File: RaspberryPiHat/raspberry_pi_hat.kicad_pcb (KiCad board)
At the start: 2 copper layers, 65 x 56 mm, 11 parts, among them J1 CONN_2x20_FEM_100PITCH_635INS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, U1 CAT24C32

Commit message: rework done
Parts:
- C1: value 100nF_0603_50V -> 100nF_CER_0603_50V
- J1: footprint JB_Header_100mils:ESQ-120-34-G-D -> ENYA_Header_100mils:ESQ-120-34-G-D

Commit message: updating project templates
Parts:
- J1: value CONN_2x20_FEM_100PITCH_635INS_280POST -> CONN_2x20_FEM_100PITCH_335INS_126POST; footprint ENYA_Header_100mils:ESQ-120-34-G-D -> ENYA_Header_100mils:PPTC202LFBN-RC; moved to F.Cu
- turned J1 to 90 degrees
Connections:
- J1 pad 10: Net-(J1-Pad10) -> (no net)
- J1 pad 11: Net-(J1-Pad11) -> (no net)
- J1 pad 12: Net-(J1-Pad12) -> (no net)
- J1 pad 13: Net-(J1-Pad13) -> (no net)
- J1 pad 15: Net-(J1-Pad15) -> (no net)
- J1 pad 16: Net-(J1-Pad16) -> (no net)
- J1 pad 18: Net-(J1-Pad18) -> (no net)
- J1 pad 19: Net-(J1-Pad19) -> (no net)
- J1 pad 21: Net-(J1-Pad21) -> (no net)
- J1 pad 22: Net-(J1-Pad22) -> (no net)
- J1 pad 23: Net-(J1-Pad23) -> (no net)
- J1 pad 24: Net-(J1-Pad24) -> (no net)
- J1 pad 26: Net-(J1-Pad26) -> (no net)
- J1 pad 29: Net-(J1-Pad29) -> (no net)
- J1 pad 3: Net-(J1-Pad3) -> (no net)
- J1 pad 31: Net-(J1-Pad31) -> (no net)
- J1 pad 32: Net-(J1-Pad32) -> (no net)
- J1 pad 33: Net-(J1-Pad33) -> (no net)
- J1 pad 35: Net-(J1-Pad35) -> (no net)
- J1 pad 36: Net-(J1-Pad36) -> (no net)
- J1 pad 37: Net-(J1-Pad37) -> (no net)
- J1 pad 38: Net-(J1-Pad38) -> (no net)
- J1 pad 40: Net-(J1-Pad40) -> (no net)
- J1 pad 5: Net-(J1-Pad5) -> (no net)
- J1 pad 7: Net-(J1-Pad7) -> (no net)
- J1 pad 8: Net-(J1-Pad8) -> (no net)

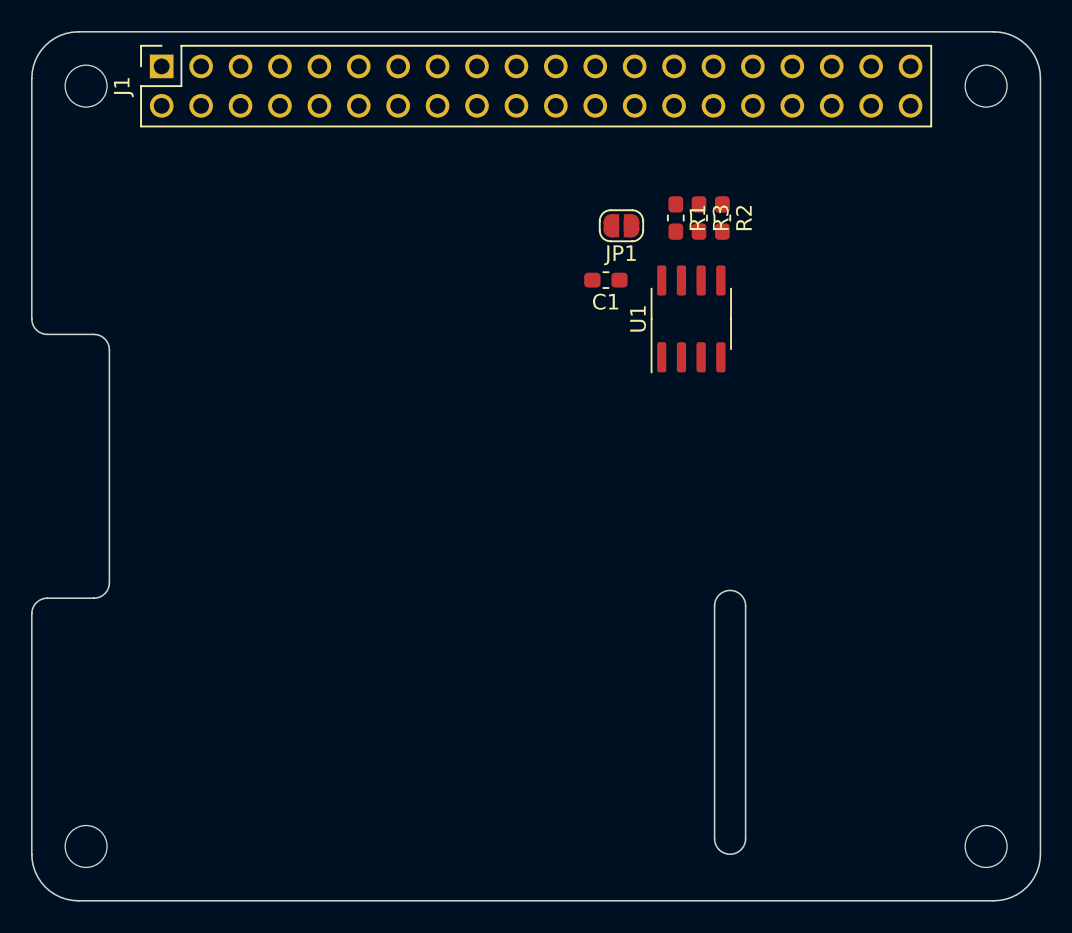
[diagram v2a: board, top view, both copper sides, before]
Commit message: migating to kicad 6
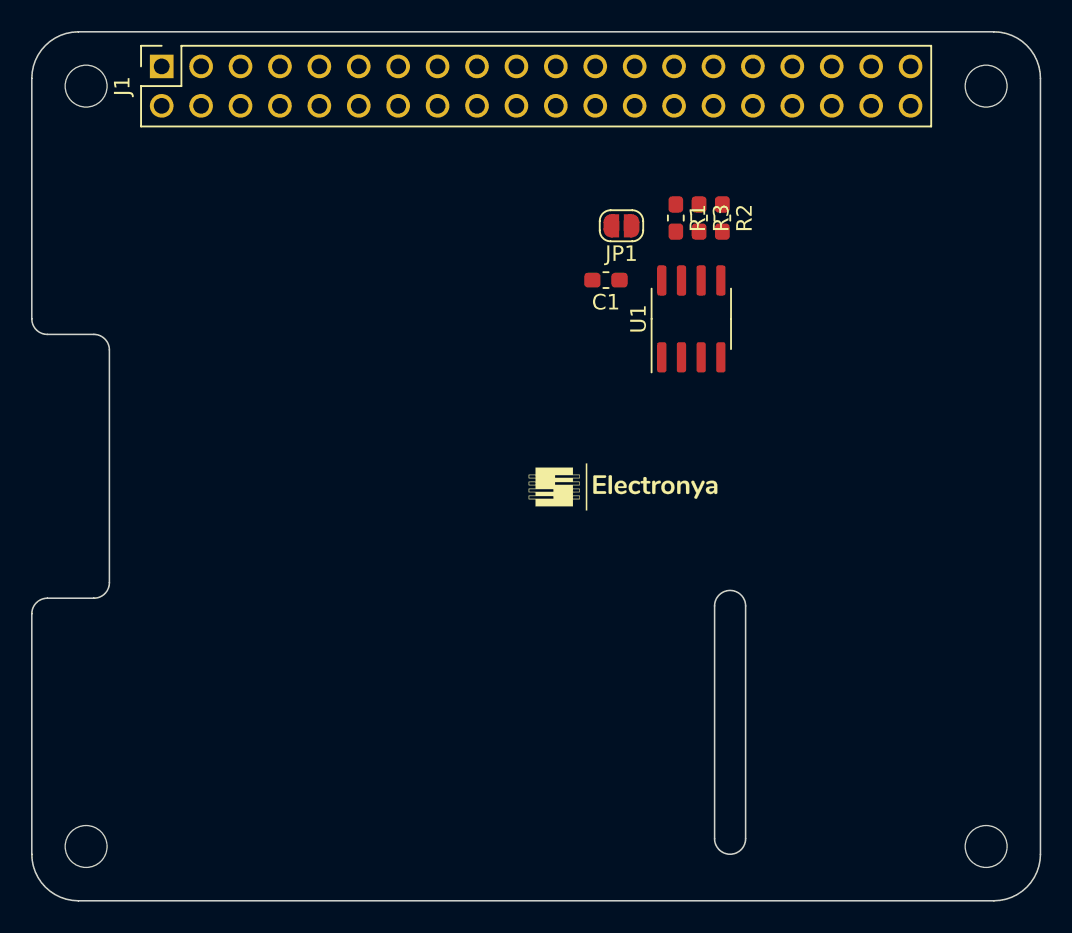
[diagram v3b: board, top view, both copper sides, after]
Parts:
- added G1: Electronya_Logo, ENYA_Bitmap:Electronya_Logo_12MM, F.Cu at (138.1, 103.3)
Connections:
- J1 pad 10: (no net) -> unconnected-(J1-Pad10)
- J1 pad 11: (no net) -> unconnected-(J1-Pad11)
- J1 pad 12: (no net) -> unconnected-(J1-Pad12)
- J1 pad 13: (no net) -> unconnected-(J1-Pad13)
- J1 pad 15: (no net) -> unconnected-(J1-Pad15)
- J1 pad 16: (no net) -> unconnected-(J1-Pad16)
- J1 pad 18: (no net) -> unconnected-(J1-Pad18)
- J1 pad 19: (no net) -> unconnected-(J1-Pad19)
- J1 pad 21: (no net) -> unconnected-(J1-Pad21)
- J1 pad 22: (no net) -> unconnected-(J1-Pad22)
- J1 pad 23: (no net) -> unconnected-(J1-Pad23)
- J1 pad 24: (no net) -> unconnected-(J1-Pad24)
- J1 pad 26: (no net) -> unconnected-(J1-Pad26)
- J1 pad 29: (no net) -> unconnected-(J1-Pad29)
- J1 pad 3: (no net) -> unconnected-(J1-Pad3)
- J1 pad 31: (no net) -> unconnected-(J1-Pad31)
- J1 pad 32: (no net) -> unconnected-(J1-Pad32)
- J1 pad 33: (no net) -> unconnected-(J1-Pad33)
- J1 pad 35: (no net) -> unconnected-(J1-Pad35)
- J1 pad 36: (no net) -> unconnected-(J1-Pad36)
- J1 pad 37: (no net) -> unconnected-(J1-Pad37)
- J1 pad 38: (no net) -> unconnected-(J1-Pad38)
- J1 pad 40: (no net) -> unconnected-(J1-Pad40)
- J1 pad 5: (no net) -> unconnected-(J1-Pad5)
- J1 pad 7: (no net) -> unconnected-(J1-Pad7)
- J1 pad 8: (no net) -> unconnected-(J1-Pad8)
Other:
- net class Default removed
